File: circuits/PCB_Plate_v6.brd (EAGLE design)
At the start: 127 x 127 mm, 158 parts, among them J1 12.0V, J10 Router V+, J11 Router V-, J12 PCONN00012, J13 MPT-08-01-01-L-RA-LC, J14 IPL1-1XX-02-XXX-DH-K-XX-MKT, J15 BOARD00012, J16 TSW1X20, J17 TSW1X20, J2 9.0V, J26 BOARD00012, J27 BOARD00012, J28 BOARD00012, J29 BOARD00012, J3 VMOTOR_A2D, J30 BOARD00012, J31 BOARD00012, J32 BOARD00012, J33 BOARD00012, J34 BOARD00012, J35 BOARD00012, J36 BOARD00012, J37 BOARD00012, J38 BOARD00012, J39 BOARD00012, J4 5.0V, J40 BOARD00012, J41 BOARD00012, J42 BOARD00012, J43 BOARD00012, J44 BOARD00012, J45 BOARD00012, J46 PCONN00012, J47 BOARD00012, J5 3.3V, J53 IMOTOR_A2D, J58 BOARD00012, J59 BOARD00012, J6 BRAINSTEMSOCKET_FEMALE, J60 BOARD00012, J68 BOARD00012, J69 BOARD00012, J71 BOARD00012, J72 GPS15X, J73 BOARD00012, J74 BOARD00012, J75 BOARD00012, J76 BOARD00012, J77 BOARD00012, J78 BOARD00012, J79 INT2, J80 INT, J81 BOARD00012, J82 BOARD00012, J83 BOARD00012, J84 BOARD00012, J85 BOARD00012, J86 BOARD00012, J87 BOARD00012, J88 BOARD00012, J89 BOARD00012, J9 GND, J90 BOARD00012, J91 BOARD00012, J92 BOARD00012, J93 BOARD00012, J94 BOARD00012, J95 BOARD00012, J96 BOARD00008, J97 BOARD00008, M1 MOUNT-HOLE3.2, M2 MOUNT-HOLE3.2, M3 MOUNT-HOLE3.2, M4 MOUNT-HOLE3.2, Q1 IXTA52P10P, Q2 IXTA52P10P, Q3 IXTA52P10P, Q4 SI4322DY, Q5 SI4322DY, Q6 IXTA52P10P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

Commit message: checking in a fully routed top plate. can one take any longer?
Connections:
- new net N$80: J17.P$16, J6.VUNREGULATED
- net BATTERY_MOTOR+_OUT: now also R4.2
- net BATTERY_MOTOR+_OUT_PRE: no longer R4.2
- net POWER_LIPO+_IN: no longer J17.P$16, J6.VUNREGULATED
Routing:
- net 5V0: track 2.54 -> 112.3 mm
- net N$2: track 1.37 -> 53.4 mm
- net BATTERY_MOTOR+_IN: track 4.39 -> 40.7 mm, vias 0 -> 2
- net BATTERY_MOTOR+_OUT: track 12.8 -> 32.0 mm
- net POWER_LIPO_POST: track 10.9 -> 29.5 mm, vias 0 -> 1
- net POWER_LIPO+_IN: track 2.54 -> 0.00 mm
- net N$80: track 0.00 -> 2.54 mm
- net GND: track 210.4 -> 210.9 mm

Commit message: checking in board. revision a ready to go
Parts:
- removed C27: PCAPI00015, aAcroname:C0603
- removed C28: T491A106K010AT, aAcroname:SMC_A
- removed C29, C30: PCAPI00016, aAcroname:C0603
- added C12: PCAPI00020, aAcroname:PANASONIC_G
- added C13: T491D227K016ZT, aAcroname:SMC_D
- added C14: CAP_POLARIZED, aAcroname:PANASONIC_NHG_A
- added C15: PCAPI00023, aAcroname:C0603
- added C17: PCAPI00007, aAcroname:C0603
- added D10, D11, D4, D5, D6, D7, D8, D9: PDIOD00003, aAcroname:LT3LR1N02-001
- added J100, J63, J99: GND, aAcroname:TSW1X1_VAL
- added J48, J49, J50, J52, J55, J56, J57, J64, J65, J66, J67, J70: BOARD00012, aAcroname:TSW1X2
- added J51: (no value), aAcroname:TSW1X1_VAL
- added J61: TSW1X20, aAcroname:TSW1X20
- added J62: VMOTOR_A2D, aAcroname:TSW1X1_VAL
- added J98: 3.3V, aAcroname:TSW1X1_VAL
- added M5, M6: MOUNT-HOLE3.2, aAcroname:3,2
- added M7: BRAINSTEM_MOUNT, avc:BRAINSTEM_MOUNT
- added R23, R24, R25, R26, R27, R28, R29, R30: PRESI00012, aAcroname:CFR-12
- added U13: NC7SZ08M5X, aAcroname:SOT23-5
- C1: value T491D227K016ZT -> ECJ-1VC1H270J; device aAcroname:SMC_D -> aAcroname:C0603
- C10, C11, C4: value PCAPI00015 -> T491D227K016ZT; device aAcroname:C0603 -> aAcroname:SMC_D
- C16: value PCAPI00020 -> PCAPI00015; device aAcroname:PANASONIC_G -> aAcroname:C0603
- C18: value T491B105K035AT -> PCAPI00015; device aAcroname:T491 -> aAcroname:C0603
- C19: value PCAPI00005 -> PCAPI00016
- C2: value T491D227K016ZT -> T491B105K035AT; device aAcroname:SMC_D -> aAcroname:T491
- C20: value PCAPI00020 -> PCAPI00016; device aAcroname:PANASONIC_G -> aAcroname:C0603
- C22: value T491B105K035AT -> T491A106K010AT; device aAcroname:T491 -> aAcroname:SMC_A
- C23: value ECJ-1VC1H270J -> PCAPI00015
- C24: value PCAPI00007 -> T491A106K010AT; device aAcroname:C0603 -> aAcroname:SMC_A
- C25: value PCAPI00023 -> PCAPI00015
- C26: value T491A106K010AT -> PCAPI00015; device aAcroname:SMC_A -> aAcroname:C0603
- C3: value CAP_POLARIZED -> T491B105K035AT; device aAcroname:PANASONIC_NHG_A -> aAcroname:T491
- C5: value CAP_POLARIZED -> PCAPI00005; device aAcroname:PANASONIC_NHG_A -> aAcroname:C0603
- C8: value T491D227K016ZT -> PCAPI00020; device aAcroname:SMC_D -> aAcroname:PANASONIC_G
- C9: value T491D227K016ZT -> CAP_POLARIZED; device aAcroname:SMC_D -> aAcroname:PANASONIC_NHG_A
- D1: value BZT52C3V3-7-F -> PDIOD00001; device aAcroname:SOD123 -> aAcroname:CHIPLED_0805
- D2: value PDIOD00001 -> BZT52C3V3-7-F; device aAcroname:CHIPLED_0805 -> aAcroname:SOD123
- J1: value 12.0V -> (none); device aAcroname:TSW1X1_VAL -> aAcroname:TSW1X1
- J10: value Router V+ -> (none); device aAcroname:TSW1X1_VAL -> aAcroname:TSW1X1
- J11: value Router V- -> (none); device aAcroname:TSW1X1_VAL -> aAcroname:TSW1X1
- J12: value PCONN00012 -> GND; device aAcroname:TSW3X4RA -> aAcroname:TSW1X1_VAL
- J13: value MPT-08-01-01-L-RA-LC -> (none); device avc:MPT-08-XX-X-RA-XX -> aAcroname:TSW1X1
- J14: value IPL1-1XX-02-XXX-DH-K-XX-MKT -> 3.3V; device avc:IPL1-110-01-S-RA -> aAcroname:TSW1X1_VAL
- J16: value TSW1X20 -> 5.0V; device aAcroname:TSW1X20 -> aAcroname:TSW1X1_VAL
- J17: value TSW1X20 -> 3.3V; device aAcroname:TSW1X20 -> aAcroname:TSW1X1_VAL
- J18, J19: value (none) -> 3.3V; device aAcroname:TSW1X1 -> aAcroname:TSW1X1_VAL
- J2: value 9.0V -> GND
- J20, J23, J25: value (none) -> BOARD00012; device aAcroname:TSW1X1 -> aAcroname:TSW1X2
- J21: value (none) -> 9.0V; device aAcroname:TSW1X1 -> aAcroname:TSW1X1_VAL
- J22: value (none) -> Router V+; device aAcroname:TSW1X1 -> aAcroname:TSW1X1_VAL
- J24: value (none) -> Router V-; device aAcroname:TSW1X1 -> aAcroname:TSW1X1_VAL
- J3: value VMOTOR_A2D -> GND
- J30: value BOARD00012 -> GPS15X; device aAcroname:TSW1X2 -> avc:GPS15
- J34: value BOARD00012 -> BRAINSTEMSOCKET_FEMALE; device aAcroname:TSW1X2 -> aAcroname:BRAINSTEMSOCKET
- J35: value BOARD00012 -> 12.0V; device aAcroname:TSW1X2 -> aAcroname:TSW1X1_VAL
- J36: value BOARD00012 -> IPL1-1XX-02-XXX-DH-K-XX-MKT; device aAcroname:TSW1X2 -> avc:IPL1-110-01-S-RA
- J37: value BOARD00012 -> TSW1X20; device aAcroname:TSW1X2 -> aAcroname:TSW1X20
- J39: value BOARD00012 -> INT; device aAcroname:TSW1X2 -> aAcroname:TSW1X1_VAL
- J4: value 5.0V -> (none); device aAcroname:TSW1X1_VAL -> aAcroname:TSW1X1
- J42, J43: value BOARD00012 -> BOARD00008; device aAcroname:TSW1X2 -> aAcroname:TSW1X1_12AWG
- J44: value BOARD00012 -> MPT-08-01-01-L-RA-LC; device aAcroname:TSW1X2 -> avc:MPT-08-XX-X-RA-XX
- J45: value BOARD00012 -> INT2; device aAcroname:TSW1X2 -> aAcroname:TSW1X1_VAL
- J46: value PCONN00012 -> BOARD00012; device aAcroname:TSW3X4RA -> aAcroname:TSW1X2
- J5: value 3.3V -> (none); device aAcroname:TSW1X1_VAL -> aAcroname:TSW1X1
- J53: value IMOTOR_A2D -> BOARD00012; device aAcroname:TSW1X1_VAL -> aAcroname:TSW1X2
- J54: device aAcroname:TSW1X1 -> aAcroname:TSW1X1_VAL
- J59: value BOARD00012 -> IMOTOR_A2D; device aAcroname:TSW1X2 -> aAcroname:TSW1X1_VAL
- J6: value BRAINSTEMSOCKET_FEMALE -> (none); device aAcroname:BRAINSTEMSOCKET -> aAcroname:TSW1X1
- J69: value BOARD00012 -> A1; device aAcroname:TSW1X2 -> aAcroname:TSW1X1_VAL
- J7, J8: device aAcroname:TSW1X1_VAL -> aAcroname:TSW1X1
- J72: value GPS15X -> A0; device avc:GPS15 -> aAcroname:TSW1X1_VAL
- J75: value BOARD00012 -> D2; device aAcroname:TSW1X2 -> aAcroname:TSW1X1_VAL
- J78: value BOARD00012 -> D1; device aAcroname:TSW1X2 -> aAcroname:TSW1X1_VAL
- J79: value INT2 -> PCONN00012; device aAcroname:TSW1X1_VAL -> aAcroname:TSW3X4RA
- J80: value INT -> BOARD00012; device aAcroname:TSW1X1_VAL -> aAcroname:TSW1X2
- J82: value BOARD00012 -> D0; device aAcroname:TSW1X2 -> aAcroname:TSW1X1_VAL
- J85: value BOARD00012 -> SCL; device aAcroname:TSW1X2 -> aAcroname:TSW1X1_VAL
- J88: value BOARD00012 -> SDA; device aAcroname:TSW1X2 -> aAcroname:TSW1X1_VAL
- J91: value BOARD00012 -> GND; device aAcroname:TSW1X2 -> aAcroname:TSW1X1_VAL
- J92: value BOARD00012 -> PCONN00012; device aAcroname:TSW1X2 -> aAcroname:TSW3X4RA
- J95: value BOARD00012 -> 5.0V; device aAcroname:TSW1X2 -> aAcroname:TSW1X1_VAL
- J96, J97: value BOARD00008 -> BOARD00012; device aAcroname:TSW1X1_12AWG -> aAcroname:TSW1X2
- Q1, Q2: value IXTA52P10P -> SI4322DY; device aAcroname:D2PACK -> aAcroname:SO-08
- Q4, Q5: value SI4322DY -> IXTA52P10P; device aAcroname:SO-08 -> aAcroname:D2PACK
- R1: value ERJ-3EKF1780V -> PRESI00006; device aAcroname:R0603@1 -> aAcroname:R0603
- R10: value PRESI00018 -> ERJ-3EKF1780V; device aAcroname:R0603 -> aAcroname:R0603@1
- R11: value PRESI00041 -> on; device aAcroname:R4527 -> aAcroname:R0603@1
- R12, R18: value PRESI00006 -> PRESI00005
- R13: value PRESI00006 -> PRESI00041; device aAcroname:R0603 -> aAcroname:R4527
- R15: value ERJ-2RKF1021X -> PRESI00018; device aAcroname:R0402 -> aAcroname:R0603
- R16: value PRESI00006 -> ERJ-2RKF9101X; device aAcroname:R0603 -> aAcroname:R0402
- R17: value ERJ-3EKF1004V -> ERJ-2RKF1021X; device aAcroname:R0603 -> aAcroname:R0402
- R2: value on -> PRESI00006; device aAcroname:R0603@1 -> aAcroname:R0603
- R22, R4: value PRESI00005 -> PRESI00006
- R3: value PRESI00006 -> ERJ-3EKF1004V
- R5: value ERJ-2RKF9101X -> PRESI00006; device aAcroname:R0402 -> aAcroname:R0603
- R6: value ERJ-3EKF1780V -> on
- R7: value on -> ERJ-3EKF1780V
- S2: value PMISC00005 -> EVQ-PE104K; device aAcroname:SPDTRA -> aAcroname:SPST-NO
- S3: value EVQ-PE104K -> PMISC00005; device aAcroname:SPST-NO -> aAcroname:SPDTRA
- U1: value (none) -> LM3150; device aAcroname:TO263-3 -> avc:TSSOP14EXP
- U10: value ADS7828E -> I2C_DIO_EXPANDER
- U11: value CMPS10 -> MCP1416; device avc:CMPS10 -> aAcroname:SOT23-5
- U12: value ADXL335 -> LTV-356T; device avc:LFCSP-16 -> aAcroname:4-SMD
- U4: value PCHIP00026 -> (none); device aAcroname:SOT23-5 -> aAcroname:TO263-3
- U5: value MCP1416 -> L3G4200DTR; device aAcroname:SOT23-5 -> avc:LGA16
- U6: value LM3150 -> ADXL335; device avc:TSSOP14EXP -> avc:LFCSP-16
- U7: value LTV-356T -> CMPS10; device aAcroname:4-SMD -> avc:CMPS10
- U8: value NC7SZ08M5X -> PCHIP00026
- U9: value L3G4200DTR -> ADS7828E; device avc:LGA16 -> aAcroname:TSSOP16
- moved M4 165.2 mm to (5.08, 5.08)
- moved M2 131.8 mm to (61.0, 121.9)
- moved R22 130.6 mm to (122.8, 12.7), turned to 180 degrees
- moved C26 124.4 mm to (119.3, 12.7), turned to 0 degrees
- moved R12 123.9 mm to (4.06, 67.1), turned to 270 degrees
- moved J14 118.9 mm to (2.54, 108.0), turned to 0 degrees
- moved M1 116.8 mm to (5.08, 121.9)
- moved M3 116.8 mm to (121.9, 121.9)
- moved U5 114.8 mm to (13.6, 63.6)
- moved R3 109.1 mm to (85.7, 115.3), turned to 270 degrees
- moved R21 105.7 mm to (116.2, 15.2), turned to 90 degrees
- moved U12 104.2 mm to (123.4, 18.7), turned to 0 degrees
- moved R20 103.4 mm to (119.3, 21.3), turned to 0 degrees
- moved J9 103.3 mm to (2.54, 113.0)
- moved C22 100.1 mm to (3.94, 59.3), turned to 90 degrees
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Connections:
- removed net N$11: J36.P$1
- removed net N$6 (its old number): R6.1, R7.2, U2.1
- new net GP2_D1: J67.P$1, J78.P$1
- new net GP2_D2: J66.P$1, J75.P$1
- new net I2C_CH0: J71.P$2, J79.P$9
- new net I2C_CH1: J74.P$2, J79.P$10
- new net I2C_CH2: J77.P$2, J79.P$11
- new net I2C_CH3: J79.P$12, J81.P$2
- new net I2C_CH4: J84.P$2, J92.P$9
- new net I2C_CH5: J87.P$2, J92.P$10
- new net I2C_CH6: J90.P$2, J92.P$11
- new net I2C_CH7: J92.P$12, J94.P$2
- new net N$101: R26.P$1, U10.7
- new net N$102: R30.P$1, U10.9
- new net N$104: R29.P$1, U10.10
- new net N$105: R28.P$1, U10.11
- new net N$108: R27.P$1, U10.12
- new net N$7: R6.2, R7.1, U2.1
- new net N$81: R23.P$1, U10.4
- new net N$82: D5.C, R24.P$2
- new net N$83: D6.C, R25.P$2
- new net N$84: D7.C, R26.P$2
- new net N$88: D11.C, R30.P$2
- new net N$89: D10.C, R29.P$2
- new net N$92: D9.C, R28.P$2
- new net N$93: D8.C, R27.P$2
- new net N$94: R24.P$1, U10.5
- new net N$95: R25.P$1, U10.6
- net !RESET: now also J34.!RESET, J37.P$1, S2.P$2; no longer J16.P$1, J6.!RESET, S3.P$2
- net 12.0V: now also C13.+, J31.P$1, J32.P$1, J33.P$1, J35.P$1, J44.5@0, J44.5@1, J44.5@2, J44.5@3, J44.5@4, J44.5@5, U4.3; no longer C1.+, J1.P$1, J13.5@0, J13.5@1, J13.5@2, J13.5@3, J13.5@4, J13.5@5, J15.P$1, J81.P$1, J82.P$1, U1.3
- net 3V3: now also C23.2, C24.+, C25.1, C26.2, D10.A, D11.A, D4.A, D5.A, D6.A, D7.A, D8.A, D9.A, J14.P$1, J15.P$1, J17.P$1, J18.P$1, J19.P$1, J29.P$2, J34.3.3V, J34.RTCV, J38.P$2, J46.P$1, J50.P$2, J53.P$2, J61.P$18, J61.P$19, J98.P$1, R19.2, R22.2, S3.3, U13.5, U9.16; no longer C10.2, C11.2, C28.+, J17.P$18, J17.P$19, J44.P$1, J5.P$1, J6.3.3V, J6.RTCV, J71.P$1, J73.P$2, J75.P$2, J85.P$2, J92.P$2, R13.2, R3.2, S1.3, U4.5
- net 5V0: now also C6.+, J16.P$1, J20.P$1, J48.P$1, J79.P$5, J79.P$6, J79.P$7, J79.P$8, J92.P$5, J92.P$6, J92.P$7, J92.P$8, J95.P$1, U2.3; no longer C8.+, J4.P$1, J43.P$1, J68.P$1, U3.3
- net 6V0: now also J52.P$1; no longer J42.P$1
- net 9.0V: now also C10.+, J21.P$1, J22.P$1, J23.P$1, U3.3; no longer C6.+, J10.P$1, J2.P$1, J69.P$1, U2.3
- net A2D0: now also J34.A2D0, J37.P$8, J57.P$1; no longer J16.P$8, J6.A2D0, J93.P$1
- net A2D1: now also J34.A2D1, J37.P$9, J56.P$1; no longer J16.P$9, J6.A2D1, J95.P$1
- net A2D2: now also J34.A2D2, J37.P$10, J55.P$1; no longer J16.P$10, J6.A2D2, J94.P$1
- net BATTERY_MOTOR+_IN: now also J44.1@0, J44.1@1, J44.1@2, J44.1@3, J44.1@4, J44.1@5, Q4.D, Q5.D, U11.2, U12.4; no longer J13.1@0, J13.1@1, J13.1@2, J13.1@3, J13.1@4, J13.1@5, Q1.D, Q2.D, U5.2, U7.4
- net BATTERY_MOTOR+_OUT: now also J43.P$1, J44.3@0, J44.3@1, J44.3@2, J44.3@3, J44.3@4, J44.3@5, R13.2, R18.2, U8.3; no longer J13.3@0, J13.3@1, J13.3@2, J13.3@3, J13.3@4, J13.3@5, J97.P$1, R11.2, R4.2, U4.3
- net BATTERY_MOTOR+_OUT_PRE: now also J42.P$1, Q4.S, Q5.S, R13.1, R16.2, U8.4; no longer J96.P$1, Q1.S, Q2.S, R11.1, R5.2, U4.4
- net DIO0: now also J34.DIO0, J61.P$1; no longer J17.P$1, J6.DIO0
- net DIO1: now also J34.DIO1, J61.P$2; no longer J17.P$2, J6.DIO1
- net DIO10: now also J34.DIO10/SDA1, J61.P$11; no longer J17.P$11, J6.DIO10/SDA1
- net DIO11: now also J34.DIO11/SCL1, J61.P$12; no longer J17.P$12, J6.DIO11/SCL1
- net DIO2: now also J34.DIO2, J61.P$3; no longer J17.P$3, J6.DIO2
- net DIO3: now also J34.DIO3, J61.P$4; no longer J17.P$4, J6.DIO3
- net DIO4: now also J34.DIO4, J61.P$5; no longer J17.P$5, J6.DIO4
- net DIO5: now also J34.DIO5, J61.P$6; no longer J17.P$6, J6.DIO5
- net DIO6: now also J34.DIO6, J61.P$7; no longer J17.P$7, J6.DIO6
- net DIO7: now also J34.DIO7, J61.P$8; no longer J17.P$8, J6.DIO7
- net DIO8: now also J34.DIO8, J61.P$9; no longer J17.P$9, J6.DIO8
- net DIO9: now also J34.DIO9, J61.P$10; no longer J17.P$10, J6.DIO9
- net ESC_EN: now also J86.P$2; no longer J29.P$2
- net GND: now also C1.2, C10.-, C11.-, C12.-, C13.-, C14.-, C16.2, C17.2, C18.2, C19.2, C20.2, C23.1, C24.-, C25.2, C26.1, C4.-, J1.P$1, J100.P$1, J2.P$1, J24.P$1, J28.P$2, J3.P$1, J34.GND, J40.P$1, J41.P$2, J44.6@0, J44.6@1, J44.6@2, J44.6@3, J44.6@4, J44.6@5, J44.8@0, J44.8@1, J44.8@2, J44.8@3, J44.8@4, J44.8@5, J51.P$1, J61.P$20, J79.P$1, J79.P$2, J79.P$3, J79.P$4, J9.P$1, J91.P$1, J92.P$1, J92.P$2, J92.P$3, J92.P$4, J99.P$1, R11.1, R12.2, R15.1, R2.2, R3.2, R6.1, S2.P$1, S3.1, U10.1, U10.2, U10.3, U10.8, U12.2, U13.3, U5.10, U5.11, U5.12, U5.13, U5.15, U5.8, U5.9, U6.3, U6.5, U6.6, U6.7, U7.GND, U8.2; no longer C1.-, C10.1, C11.1, C16.-, C18.-, C20.-, C23.2, C24.2, C26.-, C27.2, C28.-, C29.2, C30.2, C4.2, C5.-, J11.P$1, J12.P$2, J12.P$3, J12.P$4, J13.6@0, J13.6@1, J13.6@2, J13.6@3, J13.6@4, J13.6@5, J13.8@0, J13.8@1, J13.8@2, J13.8@3, J13.8@4, J13.8@5, J17.P$20, J25.P$1, J45.P$1, J46.P$1, J46.P$2, J46.P$3, J46.P$4, J6.GND, J74.P$2, J8.P$1, J86.P$2, R10.1, R17.2, R19.2, R2.1, R22.2, R7.1, S2.1, S3.P$1, U10.11, U10.12, U10.13, U10.9, U11.GND, U12.3, U12.5, U12.6, U12.7, U4.2, U7.2, U8.3, U9.10, U9.15, U9.8
- net GND3: now also J44.2@0, J44.2@1, J44.2@2, J44.2@3, J44.2@4, J44.2@5, J44.4@0, J44.4@1, J44.4@2, J44.4@3, J44.4@4, J44.4@5, J63.P$1, R17.1, R20.1, U11.4; no longer J13.2@0, J13.2@1, J13.2@2, J13.2@3, J13.2@4, J13.2@5, J13.4@0, J13.4@1, J13.4@2, J13.4@3, J13.4@4, J13.4@5, J9.P$1, R12.1, R15.1, U5.4
- net IMOTOR_A2D: now also J54.P$1, J59.P$1, R15.2, U8.1; no longer J53.P$1, J7.P$1, R10.2, U4.1
- net N$1: now also R10.1, R11.2, U4.1; no longer R1.1, R2.2, U1.1
- net N$100: now also C16.1, J38.P$1, U6.14, U6.15; no longer C4.1, J92.P$1, U12.14, U12.15
- net N$103: now also C19.1, J55.P$2, U6.8; no longer C21.1, J93.P$2, U12.8
- net N$106: now also J20.P$2, R8.2, U3.2, U3.TAB; no longer J68.P$2, R6.2, U2.2, U2.TAB
- net N$107: now also C11.+, J23.P$2, R10.2, U4.2, U4.TAB; no longer C2.+, J69.P$2, R1.2, U1.2, U1.TAB
- net N$109: now also C4.+, J15.P$2, R7.2, U2.2, U2.TAB; no longer C9.+, J71.P$2, R8.2, U3.2, U3.TAB
- net N$110: now also C20.1, J56.P$2, U6.10; no longer C29.1, J95.P$2, U12.10
- net N$111: now also C21.1, J57.P$2, U6.12; no longer C30.1, J94.P$2, U12.12
- net N$12: now also J34.WATCHDOG, J61.P$13; no longer J17.P$13, J6.WATCHDOG
- net N$13: now also D4.C, R23.P$2; no longer J37.P$1
- net N$14: now also J65.P$1; no longer J38.P$1
- net N$15: now also J64.P$1; no longer J39.P$1
- net N$16: now also J34.PE_0, J37.P$2; no longer J16.P$2, J6.PE_0
- net N$17: now also J34.PE_1, J37.P$3; no longer J16.P$3, J6.PE_1
- net N$18: now also J34.PE_2, J37.P$4; no longer J16.P$4, J6.PE_2
- net N$19: now also J34.PE_3, J37.P$5; no longer J16.P$5, J6.PE_3
- net N$2: now also S1.2, U1.3; no longer S2.2, U6.3
- net N$20: now also J34.PE_4, J37.P$6; no longer J16.P$6, J6.PE_4
- net N$21: now also J34.DAC, J37.P$7; no longer J16.P$7, J6.DAC
- net N$22: now also J34.UART1_RX_LED, J37.P$11; no longer J16.P$11, J6.UART1_RX_LED
- net N$23: now also J34.UART1_TX_LED, J37.P$12; no longer J16.P$12, J6.UART1_TX_LED
- net N$24: now also J41.P$1, U7.MODE; no longer J86.P$1, U11.MODE
- net N$25: now also J71.P$1, U9.1; no longer J58.P$1, U10.1
- net N$26: now also J34.UART0_RX_LED, J37.P$15; no longer J16.P$15, J6.UART0_RX_LED
- net N$27: now also J34.UART0_TX_LED, J37.P$16; no longer J16.P$16, J6.UART0_TX_LED
- net N$28: now also C18.1, C22.+, J50.P$1, U5.1, U5.16; no longer C26.+, C27.1, J73.P$1, U9.1, U9.16
- net N$29: now also R14.1, U5.5; no longer R21.1, U9.5
- net N$3: now also Q4.G, Q5.G, U11.5; no longer Q1.G, Q2.G, U5.5
- net N$30: now also J34.T0, J37.P$19; no longer J16.P$19, J6.T0
- net N$31: now also J34.T1, J37.P$20; no longer J16.P$20, J6.T1
- net N$32: now also J29.P$1, J30.BACKUPPWR, J30.PWR; no longer J72.BACKUPPWR, J72.PWR, J75.P$1
- net N$33: now also J28.P$1, J30.GND; no longer J72.GND, J74.P$1
- net N$34: now also J27.P$1, J30.STX; no longer J72.STX, J76.P$1
- net N$35: now also J26.P$1, J30.SRX; no longer J72.SRX, J77.P$1
- net N$36: now also J25.P$1, J30.RFBIAS; no longer J72.RFBIAS, J78.P$1
- net N$37: now also C15.2, C17.1, U5.14; no longer C24.1, C25.2, U9.14
- net N$38: now also C15.1, R12.1; no longer C25.1, R22.1
- net N$39: now also J39.P$1, U5.7; no longer J80.P$1, U9.7
- net N$4: now also R18.1; no longer R4.1
- net N$40: now also J45.P$1, U5.6; no longer J79.P$1, U9.6
- net N$41: now also U9.10; no longer U10.10
- net N$42: now also C12.+, C14.+, J10.P$1, J31.P$2, J32.P$2, J33.P$2, R4.1; no longer C20.+, C5.+, J15.P$2, J22.P$1, J81.P$2, J82.P$2, R18.1
- net N$43: now also J53.P$1, U7.3.3V; no longer J85.P$1, U11.3.3V
- net N$44: now also J34.VTRANSPORT, J61.P$17; no longer J17.P$17, J6.VTRANSPORT
- net N$45: now also C2.+, C3.+, U1.1; no longer C18.+, C22.+, U6.1
- net N$46: now also J36.1, J96.P$1; no longer J14.1, J26.P$1
- net N$47: now also Q1.1, Q1.2, Q1.3, U1.14, U1.5, U1.9, U1.PAD; no longer Q5.1, Q5.2, Q5.3, U6.14, U6.5, U6.9, U6.PAD
- net N$48: now also Q1.4, U1.13; no longer Q5.4, U6.13
- net N$49: now also Q2.4, U1.11; no longer Q4.4, U6.11
- net N$5: now also R22.1, U12.1, U13.4; no longer R3.1, U7.1, U8.4
- net N$50: now also R3.1; no longer R17.1
- net N$51: now also J4.P$1, R1.2, U1.7; no longer J20.P$1, R16.2, U6.7
- net N$52: now also C5.1, J11.P$1, J13.P$1, Q1.5, Q1.6, Q1.7, Q1.8, Q2.1, Q2.2, Q2.3, R5.2, U1.10; no longer C19.1, J19.P$1, J54.P$1, Q4.1, Q4.2, Q4.3, Q5.5, Q5.6, Q5.7, Q5.8, R20.2, U6.10
- net N$53: now also C5.2, U1.12; no longer C19.2, U6.12
- net N$54: now also J6.P$1, J7.P$1, R2.1, R4.2, U1.4; no longer J23.P$1, J24.P$1, R18.2, R19.1, U6.4
- net N$55: now also J8.P$1, R5.1, U1.8; no longer J18.P$1, R20.1, U6.8
- net N$56: now also J36.2, J93.P$1; no longer J14.2, J27.P$1
- net N$57: now also J36.3, J89.P$1; no longer J14.3, J28.P$1
- net N$58: now also C1.1, U1.6; no longer C23.1, U6.6
- net N$59: now also J36.4, J86.P$1; no longer J14.4, J29.P$1
- net N$60: now also J36.5, J83.P$1; no longer J14.5, J30.P$1
- net N$61: now also J36.6, J80.P$1; no longer J14.6, J31.P$1
- net N$62: now also J36.7, J76.P$1; no longer J14.7, J32.P$1
- net N$63: now also J36.8, J73.P$1; no longer J14.8, J33.P$1
- net N$64: now also J36.9, J70.P$1; no longer J14.9, J34.P$1
- net N$65: now also J36.10, J68.P$1; no longer J14.10, J35.P$1
- net N$66: now also J60.P$1; no longer J40.P$1
- net N$67: now also J58.P$1; no longer J41.P$1
- net N$68: now also J36.20, J67.P$2; no longer J14.20, J36.P$2
- net N$69: now also J36.19, J66.P$2; no longer J14.19, J37.P$2
- net N$70: now also J36.18, J65.P$2; no longer J14.18, J38.P$2
- net N$71: now also J36.17, J64.P$2; no longer J14.17, J39.P$2
- net N$72: now also J36.16, J60.P$2; no longer J14.16, J40.P$2
- net N$73: now also J36.15, J58.P$2; no longer J14.15, J41.P$2
- net N$74: now also J36.14, J52.P$2; no longer J14.14, J42.P$2
- net N$75: now also J36.13, J48.P$2; no longer J14.13, J43.P$2
- net N$76: now also J36.12, J46.P$2; no longer J14.12, J44.P$2
- net N$77: now also J36.11, J40.P$2; no longer J14.11, J45.P$2
- net N$78: now also J97.P$1, R21.1, U13.2; no longer J47.P$1, R13.1, U8.2
- net N$79: now also R20.2, U11.3, U12.3; no longer R12.2, U5.3, U7.3
- net N$8: now also S3.2, U13.1; no longer S1.2, U8.1
- net N$80: now also J34.VUNREGULATED, J61.P$16; no longer J17.P$16, J6.VUNREGULATED
- net N$85: now also J49.P$1, U7.TX; no longer J84.P$1, U11.TX
- net N$86: now also J47.P$1, U7.RX; no longer J83.P$1, U11.RX
- net N$87: now also J74.P$1, U9.2; no longer J59.P$1, U10.2
- net N$9: now also R19.1; no longer R14.1
- net N$90: now also J77.P$1, U9.3; no longer J60.P$1, U10.3
- net N$91: now also J81.P$1, U9.4; no longer J87.P$1, U10.4
- net N$96: now also J84.P$1, U9.5; no longer J88.P$1, U10.5
- net N$97: now also J87.P$1, U9.6; no longer J89.P$1, U10.6
- net N$98: now also U9.7; no longer U10.7
- net N$99: now also J94.P$1, U9.8; no longer J91.P$1, U10.8
- net POWER_LIPO+_IN: now also J44.7@0, J44.7@1, J44.7@2, J44.7@3, J44.7@4, J44.7@5; no longer J13.7@0, J13.7@1, J13.7@2, J13.7@3, J13.7@4, J13.7@5
- net POWER_LIPO_POST: now also C8.+, C9.+, J5.P$1, Q2.5, Q2.6, Q2.7, Q2.8, R1.1, U1.2; no longer C16.+, C3.+, J21.P$1, Q4.5, Q4.6, Q4.7, Q4.8, R16.1, U6.2
- net QUAD0A: now also J83.P$2; no longer J30.P$2
- net QUAD0B: now also J80.P$2; no longer J31.P$2
- net QUAD1A: now also J76.P$2; no longer J32.P$2
- net QUAD1B: now also J73.P$2; no longer J33.P$2
- net SCL: now also J34.SCL, J61.P$15, J68.P$2, J85.P$1, U5.2, U9.14; no longer J17.P$15, J35.P$2, J6.SCL, U9.2
- net SDA: now also J34.SDA, J61.P$14, J70.P$2, J88.P$1, U5.3, U9.15; no longer J17.P$14, J34.P$2, J6.SDA, U9.3
- net SPM2: now also J89.P$2; no longer J28.P$2
- net SPWM0: now also J96.P$2; no longer J26.P$2
- net SPWM1: now also J93.P$2; no longer J27.P$2
- net SRX0: now also J27.P$2, J34.UART0_RX, J37.P$17; no longer J16.P$17, J6.UART0_RX, J76.P$2
- net SRX1: now also J34.UART1_RX, J37.P$13, J49.P$2; no longer J16.P$13, J6.UART1_RX, J84.P$2
- net STX0: now also J26.P$2, J34.UART0_TX, J37.P$18; no longer J16.P$18, J6.UART0_TX, J77.P$2
- net STX1: now also J34.UART1_TX, J37.P$14, J47.P$2; no longer J16.P$14, J6.UART1_TX, J83.P$2
- net VMOTOR_A2D: now also J62.P$1, R16.1, R17.2; no longer J3.P$1, R15.2, R5.1
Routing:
- net 5V0: track 112.3 -> 178.4 mm, vias 0 -> 2
- net GND: track 210.9 -> 153.4 mm, vias 18 -> 19
- net SDA: track 65.6 -> 116.6 mm, vias 1 -> 2
- net SCL: track 77.0 -> 121.2 mm, vias 1 -> 4
- net A2D0: track 5.08 -> 31.9 mm
- net A2D1: track 5.08 -> 29.7 mm, vias 0 -> 1
- net A2D2: track 5.08 -> 27.4 mm
- net N$81: track 0.00 -> 20.4 mm
- net N$102: track 0.00 -> 20.3 mm
- net GP2_D1: track 0.00 -> 20.2 mm
- net GP2_D2: track 0.00 -> 18.8 mm
- net N$94: track 0.00 -> 16.5 mm
- net N$104: track 0.00 -> 16.3 mm
- net N$108: track 0.00 -> 13.4 mm
- net N$105: track 0.00 -> 12.9 mm
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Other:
- board text added: "3.3V"
- board text added: "A2D0_I2C"
- board text added: "A2D1_I2C"
- board text added: "A2D2_I2C"
- board text added: "A2D3_I2C"
- board text added: "A2D4_I2C"
- board text added: "A2D5_I2C"
- board text added: "A2D6_I2C"
- board text added: "A2D7_I2C"
- board text added: "GND"
- board text added: "Headless Chicken Revision A"
- board text added: "Logic Power Enable"
- board text added: "Motor Power Enable"
- board text added: "SCL"
- board text added: "SDA"

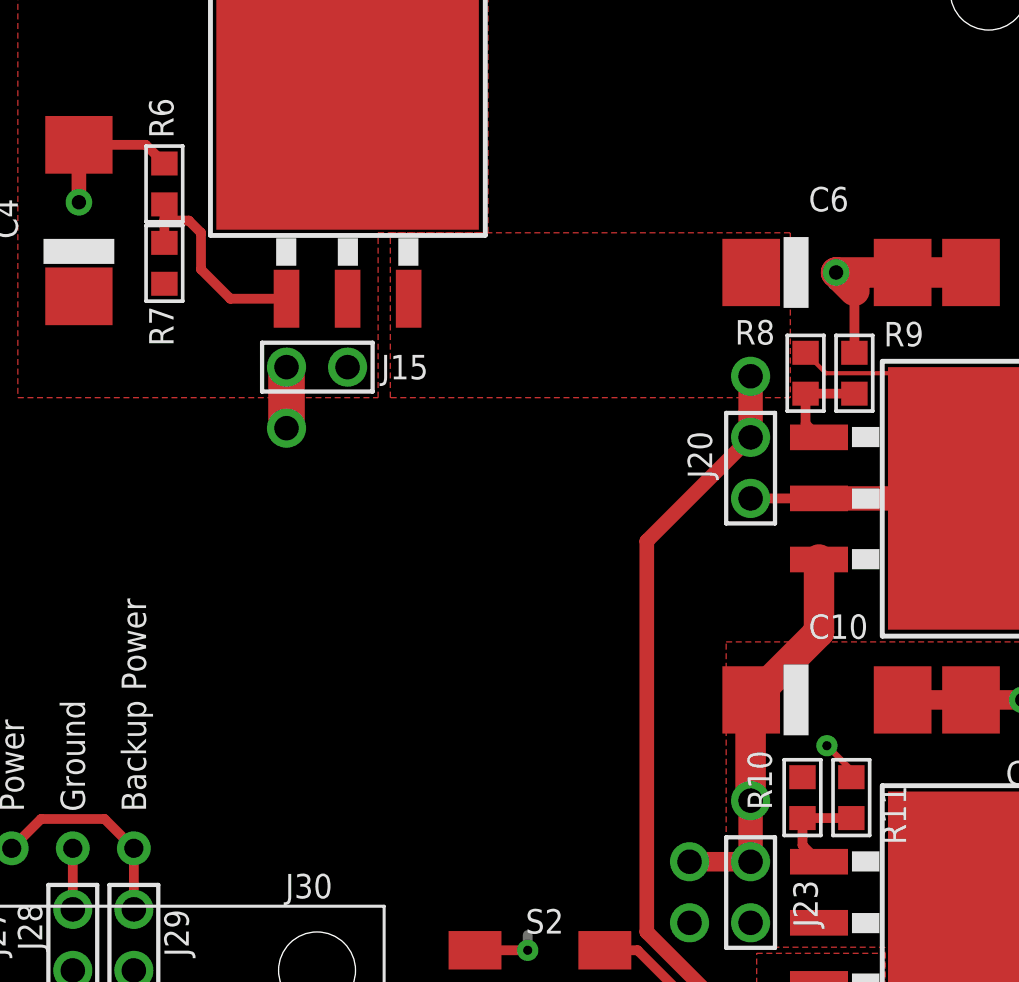
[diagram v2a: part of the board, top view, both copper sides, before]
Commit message: updated part numbers
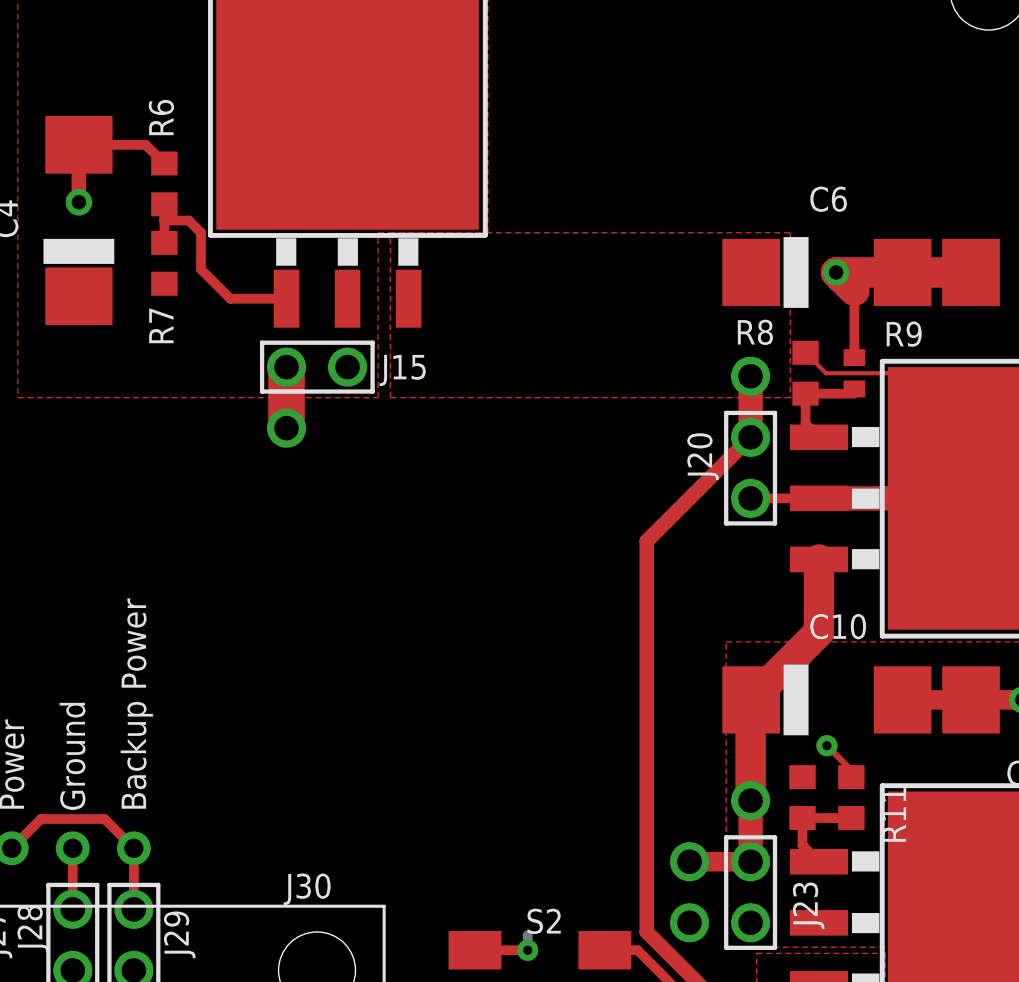
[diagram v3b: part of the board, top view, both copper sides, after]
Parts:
- R10: value ERJ-3EKF1780V -> PRESI00039; device aAcroname:R0603@1 -> aAcroname:R0603
- R11, R6: device aAcroname:R0603@1 -> aAcroname:R0603
- R7: value ERJ-3EKF1780V -> PRESI00007; device aAcroname:R0603@1 -> aAcroname:R0603
- R8: value ERJ-3EKF1780V -> PRESI00019; device aAcroname:R0603@1 -> aAcroname:R0603
- R9: device aAcroname:R0603@1 -> aAcroname:R0402
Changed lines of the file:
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@@
 <attribute name="NAME" x="56.388" y="77.343" size="1.016" layer="25" font="vector" ratio="13"/>
 </element>
-<element name="R10" library="aAcroname" package="R0603@1" value="ERJ-3EKF1780V" x="53.213" y="88.392" locked="yes" smashed="yes" rot="R90">
-<attribute name="ACRONAME" value="PRESI00036" x="53.213" y="88.392" size="1.778" layer="27" rot="R90" display="off"/>
+<element name="R10" library="aAcroname" package="R0603" value="PRESI00039" x="53.213" y="88.392" locked="yes" smashed="yes" rot="R90">
+<attribute name="ACRONAME" value="PRESI00039" x="53.213" y="88.392" size="1.778" layer="27" rot="R90" display="off"/>
 <attribute name="NOTES" value="" x="53.213" y="88.392" size="1.778" layer="27" rot="R90" display="off"/>
-<attribute name="PARTNUM" value="ERJ-3EKF1780V" x="53.213" y="88.392" size="1.778" layer="27" rot="R90" display="off"/>
-<attribute name="NAME" x="51.943" y="87.884" size="1.016" layer="25" font="vector" ratio="13" rot="R90"/>
+<attribute name="PARTNUM" value="ERJ-3EKF6980V" x="53.213" y="88.392" size="1.778" layer="27" rot="R90" display="off"/>
 </element>
-<element name="R11" library="aAcroname" package="R0603@1" value="on" x="55.245" y="88.392" locked="yes" smashed="yes" rot="R270">
+<element name="R11" library="aAcroname" package="R0603" value="on" x="55.245" y="88.392" locked="yes" smashed="yes" rot="R270">
 <attribute name="ACRONAME" value="-" x="55.245" y="88.392" size="1.778" layer="27" rot="R270" display="off"/>
 <attribute name="NOTES" value="" x="55.245" y="88.392" size="1.778" layer="27" rot="R270" display="off"/>
 <attribute name="PARTNUM" value="ERJ-3EKF3830V" x="55.245" y="88.392" size="1.778" layer="27" rot="R270" display="off"/>
 <attribute name="NAME" x="56.515" y="88.9" size="1.016" layer="25" font="vector" ratio="13" rot="R270"/>
+<attribute name="CVALUE" value="" x="55.245" y="88.392" size="1.778" layer="27" rot="R270" display="off"/>
+<attribute name="RESISTANCE" value="4.22k" x="55.245" y="88.392" size="1.778" layer="27" rot="R270" display="off"/>
 </element>
 <element name="C11" library="aAcroname" package="SMC_D" value="T491D227K016ZT" x="63.373" y="92.456" locked="yes" smashed="yes" rot="R180">
@@
 <attribute name="NAME" x="53.467" y="94.996" size="1.016" layer="25" font="vector" ratio="13"/>
 </element>
-<element name="R8" library="aAcroname" package="R0603@1" value="ERJ-3EKF1780V" x="53.34" y="106.045" locked="yes" smashed="yes" rot="R90">
-<attribute name="ACRONAME" value="PRESI00036" x="53.34" y="106.045" size="1.778" layer="27" rot="R90" display="off"/>
+<element name="R8" library="aAcroname" package="R0603" value="PRESI00019" x="53.34" y="106.045" locked="yes" smashed="yes" rot="R90">
+<attribute name="ACRONAME" value="PRESI00019" x="53.34" y="106.045" size="1.778" layer="27" rot="R90" display="off"/>
 <attribute name="NOTES" value="" x="53.34" y="106.045" size="1.778" layer="27" rot="R90" display="off"/>
-<attribute name="PARTNUM" value="ERJ-3EKF1780V" x="53.34" y="106.045" size="1.778" layer="27" rot="R90" display="off"/>
+<attribute name="PARTNUM" value="ERJ-3EKF2431V" x="53.34" y="106.045" size="1.778" layer="27" rot="R90" display="off"/>
 <attribute name="NAME" x="52.07" y="108.2548" size="1.016" layer="25" font="vector" ratio="13" rot="R180"/>
+<attribute name="UNITCOST" value="0.006" x="53.34" y="106.045" size="1.778" layer="27" rot="R90" display="off"/>
 </element>
-<element name="R9" library="aAcroname" package="R0603@1" value="on" x="55.372" y="106.045" locked="yes" smashed="yes" rot="R270">
-<attribute name="ACRONAME" value="-" x="55.372" y="106.045" size="1.778" layer="27" rot="R270" display="off"/>
+<element name="R9" library="aAcroname" package="R0402" value="on" x="55.372" y="106.045" locked="yes" smashed="yes" rot="R270">
+<attribute name="ACRONAME" value="PRESI00056" x="55.372" y="106.045" size="1.778" layer="27" rot="R270" display="off"/>
 <attribute name="NOTES" value="" x="55.372" y="106.045" size="1.778" layer="27" rot="R270" display="off"/>
-<attribute name="PARTNUM" value="ERJ-3EKF3830V" x="55.372" y="106.045" size="1.778" layer="27" rot="R270" display="off"/>
+<attribute name="PARTNUM" value="ERJ-3EKF6491V" x="55.372" y="106.045" size="1.778" layer="27" rot="R270" display="off"/>
 <attribute name="NAME" x="56.5912" y="107.1626" size="1.016" layer="25" font="vector" ratio="13"/>
+<attribute name="UNITCOST" value="0.006" x="55.372" y="106.045" size="1.778" layer="27" rot="R270" display="off"/>
 </element>
 <element name="C7" library="aAcroname" package="SMC_D" value="T491D227K016ZT" x="63.373" y="110.236" locked="yes" smashed="yes" rot="R180">
@@
 <attribute name="NAME" x="53.467" y="112.776" size="1.016" layer="25" font="vector" ratio="13"/>
 </element>
-<element name="R7" library="aAcroname" package="R0603@1" value="ERJ-3EKF1780V" x="26.67" y="110.617" locked="yes" smashed="yes" rot="R270">
-<attribute name="ACRONAME" value="PRESI00036" x="26.67" y="110.617" size="1.778" layer="27" rot="R270" display="off"/>
+<element name="R7" library="aAcroname" package="R0603" value="PRESI00007" x="26.67" y="110.617" locked="yes" smashed="yes" rot="R270">
+<attribute name="ACRONAME" value="PRESI00007" x="26.67" y="110.617" size="1.778" layer="27" rot="R270" display="off"/>
 <attribute name="NOTES" value="" x="26.67" y="110.617" size="1.778" layer="27" rot="R270" display="off"/>
-<attribute name="PARTNUM" value="ERJ-3EKF1780V" x="26.67" y="110.617" size="1.778" layer="27" rot="R270" display="off"/>
+<attribute name="PARTNUM" value="ERJ-3GEYJ222V" x="26.67" y="110.617" size="1.778" layer="27" rot="R270" display="off"/>
 <attribute name="NAME" x="26.035" y="108.839" size="1.016" layer="25" font="vector" ratio="13" rot="R270"/>
+<attribute name="UNITCOST" value="" x="26.67" y="110.617" size="1.778" layer="27" rot="R270" display="off"/>
 </element>
-<element name="R6" library="aAcroname" package="R0603@1" value="on" x="26.67" y="113.919" locked="yes" smashed="yes" rot="R270">
-<attribute name="ACRONAME" value="-" x="26.67" y="113.919" size="1.778" layer="27" rot="R270" display="off"/>
+<element name="R6" library="aAcroname" package="R0603" value="on" x="26.67" y="113.919" locked="yes" smashed="yes" rot="R270">
+<attribute name="ACRONAME" value="PRESI00002" x="26.67" y="113.919" size="1.778" layer="27" rot="R270" display="off"/>
 <attribute name="NOTES" value="" x="26.67" y="113.919" size="1.778" layer="27" rot="R270" display="off"/>
-<attribute name="PARTNUM" value="ERJ-3EKF3830V" x="26.67" y="113.919" size="1.778" layer="27" rot="R270" display="off"/>
+<attribute name="PARTNUM" value="ERJ-3GEYJ332V" x="26.67" y="113.919" size="1.778" layer="27" rot="R270" display="off"/>
 <attribute name="NAME" x="27.051" y="115.824" size="1.016" layer="25" font="vector" ratio="13" rot="R90"/>
 </element>

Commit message: checking in schematic changes
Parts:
- R16, R17: device aAcroname:R0402 -> aAcroname:R0402@1
